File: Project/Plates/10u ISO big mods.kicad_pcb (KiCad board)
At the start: 2 copper layers, 257.2 x 76.2 mm, 45 parts

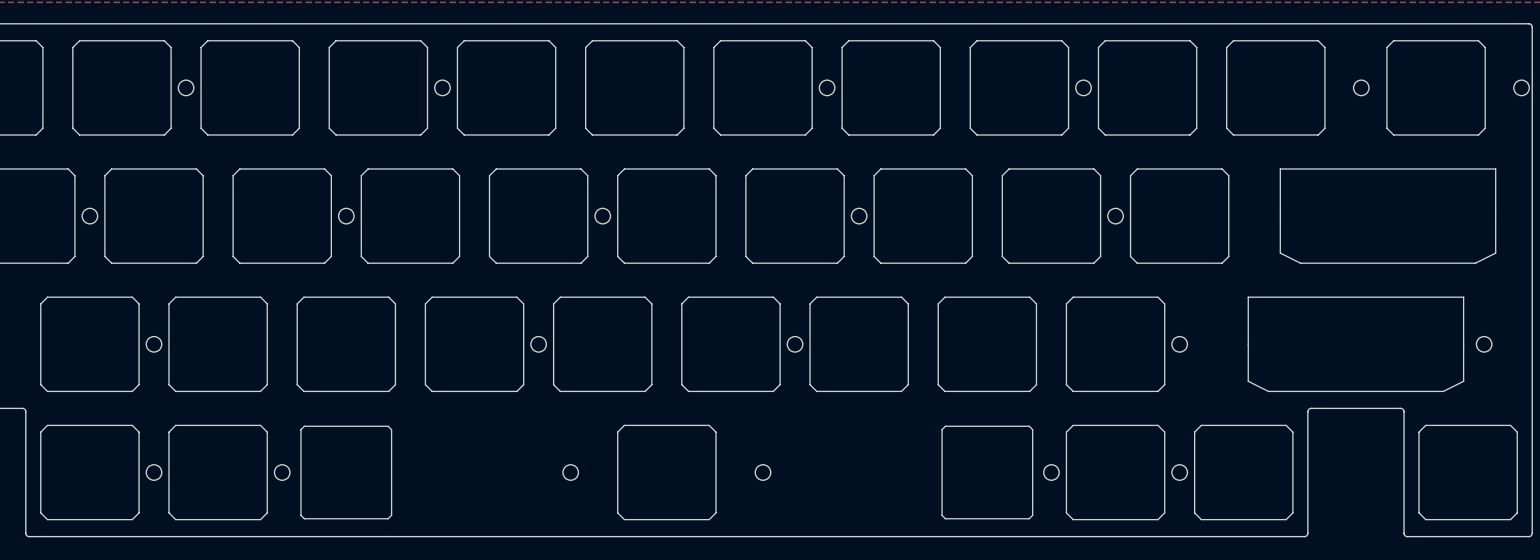
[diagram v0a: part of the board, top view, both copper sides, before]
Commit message: bottom row change, plate update, firmware update
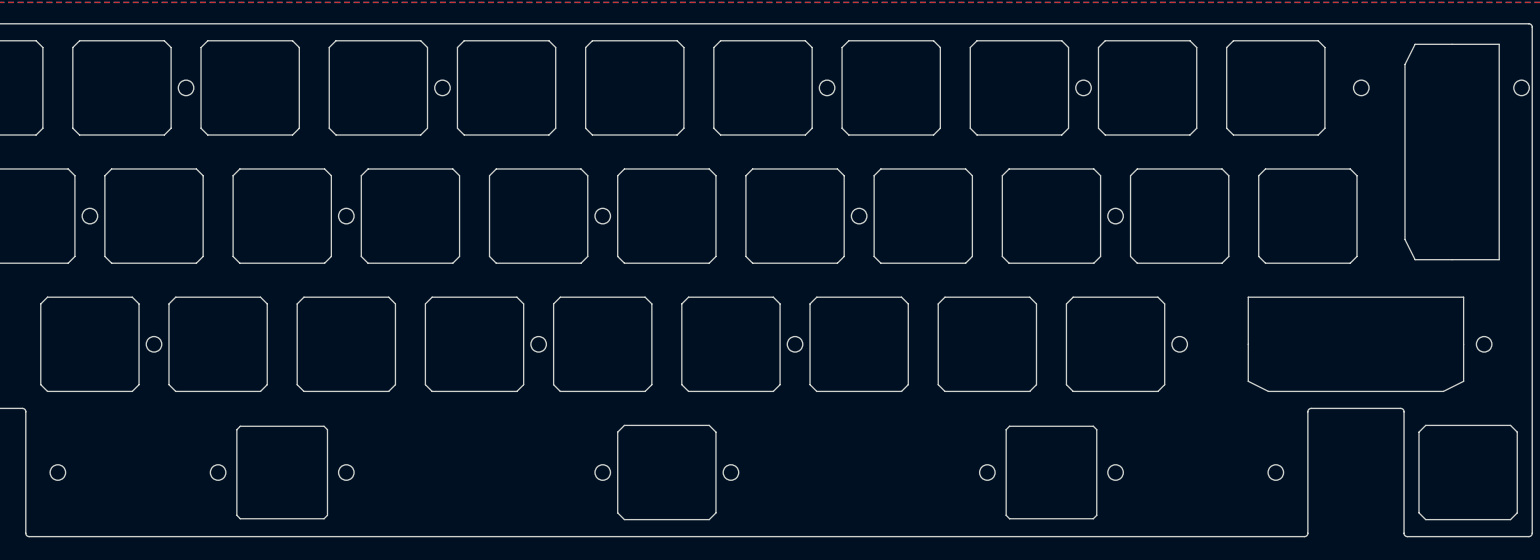
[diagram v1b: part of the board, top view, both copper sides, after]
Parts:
- removed the REF** at (260.4, 34.1)
- removed the REF** at (146.1, 91.3) (x2)
- removed the REF** at (79.4, 91.3)
- removed the REF** at (212.7, 91.3)
- removed the REF** at (60.3, 91.3)
- removed the REF** at (231.8, 91.3)
- added REF**: Value, cipulot_parts:ecs_7U_space_stab, F.Cu at (146.1, 91.3)
- added REF**: Value, cipulot_parts:ecs_plate_cut_1U, F.Cu at (241.3, 53.2)
- added REF**: Value, cipulot_parts:ecs_plate_cut_7U_space_stab, F.Cu at (146.1, 91.3)
- moved REF** 13.5 mm to (262.7, 43.7), turned to -90 degrees
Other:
- outline, holes or cut-outs redrawn
- board text added: "REF**"
- board text added: "SW_EC39"
